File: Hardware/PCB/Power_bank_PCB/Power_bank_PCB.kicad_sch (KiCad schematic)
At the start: 86 parts, among them IC1 TPS63070RNMR, IC2 TPS63070RNMR, J1 Fotopanel_connector, J2 Vout, J3 Alterative_charging, Q1 8205A, Q2 2N7002, Q3 DMP3099L, U1 TP4056-42-ESOP8, U2 MCP4018-xxxxLT, U3 DW01A, U4 STM32U031F8Px, U5 INA219AxD, U6 TPS61022

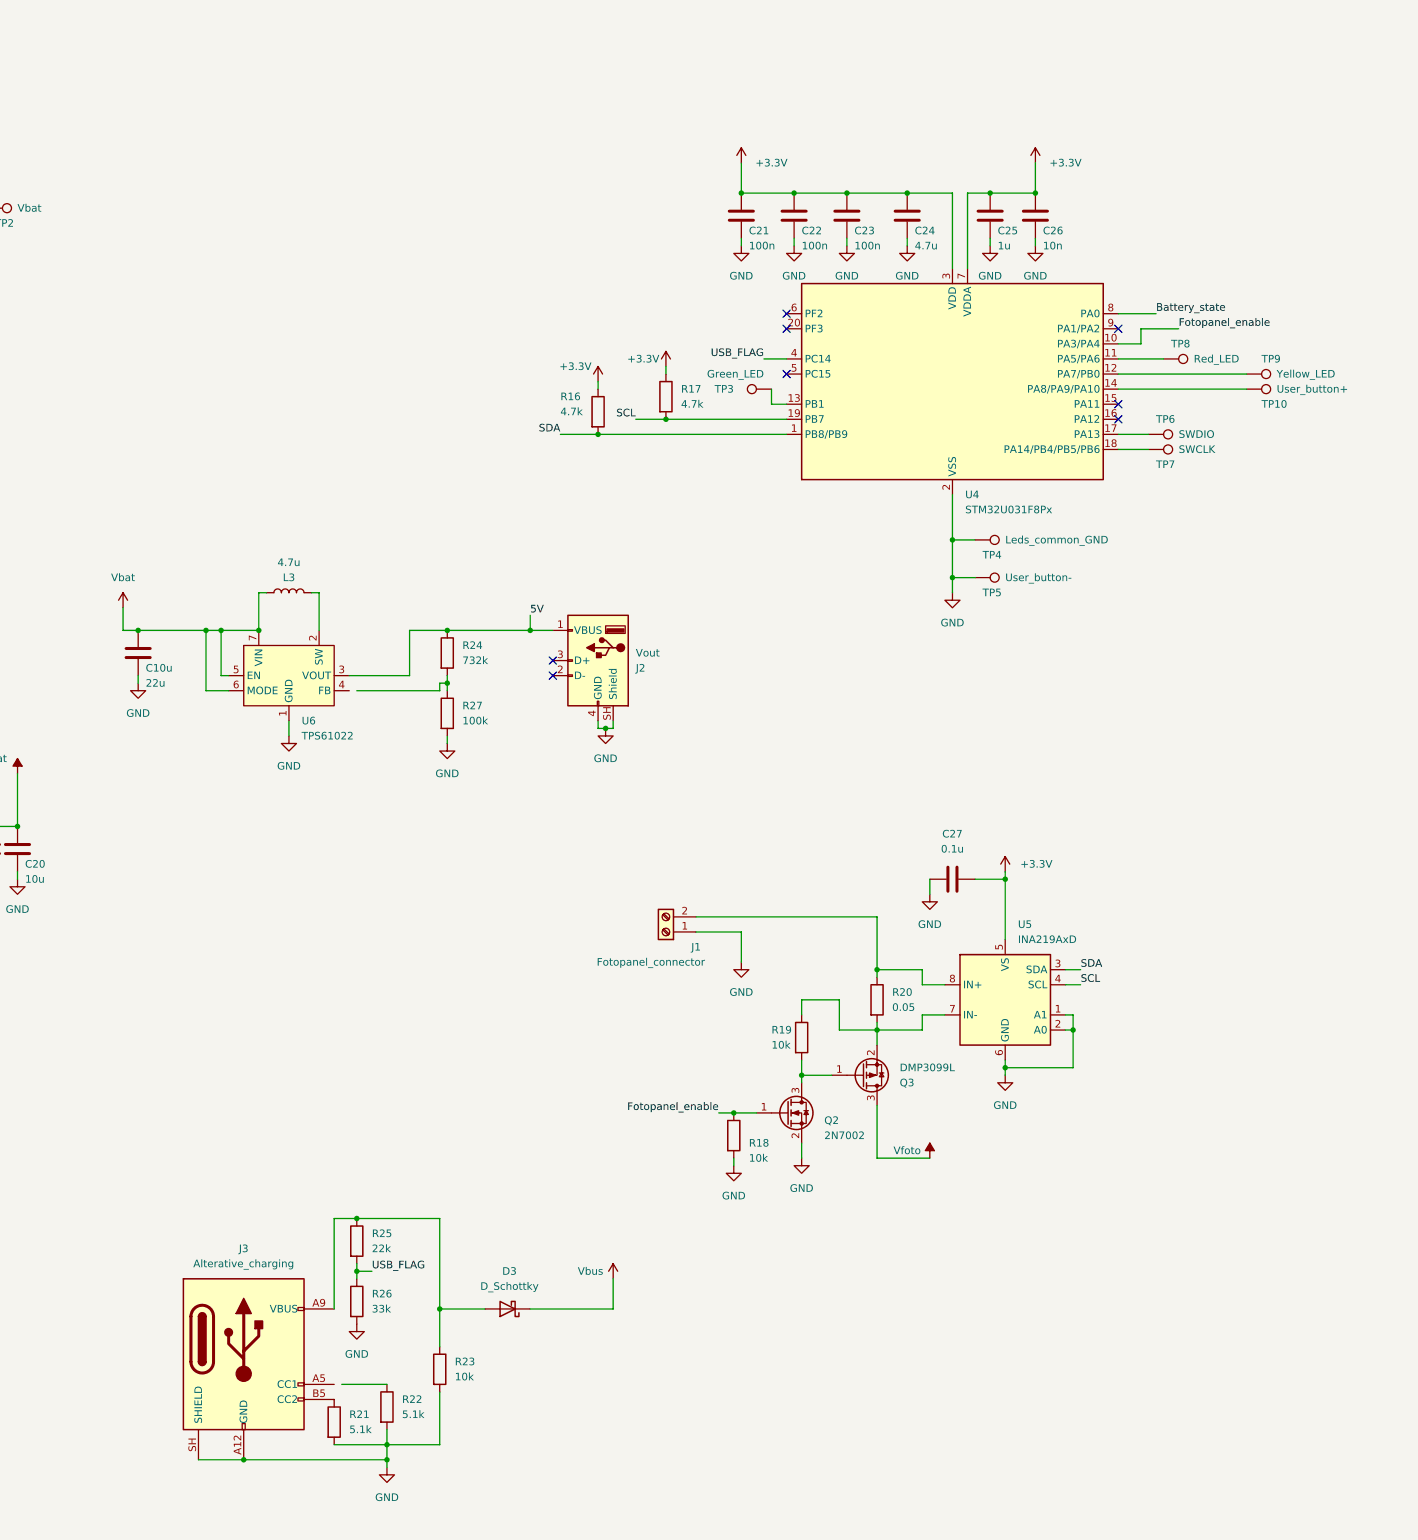
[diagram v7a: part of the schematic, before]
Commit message: Adjust schematic positions
Mass-update schematic component and net coordinates to match revised layout (many junctions, wires, labels and symbol positions changed). Add a +3.3V power symbol instance (#PWR064) and update used_designators (R21-29, D3-5, #PWR54-64, etc.). These changes align the schematic with the updated PCB placement and nets.
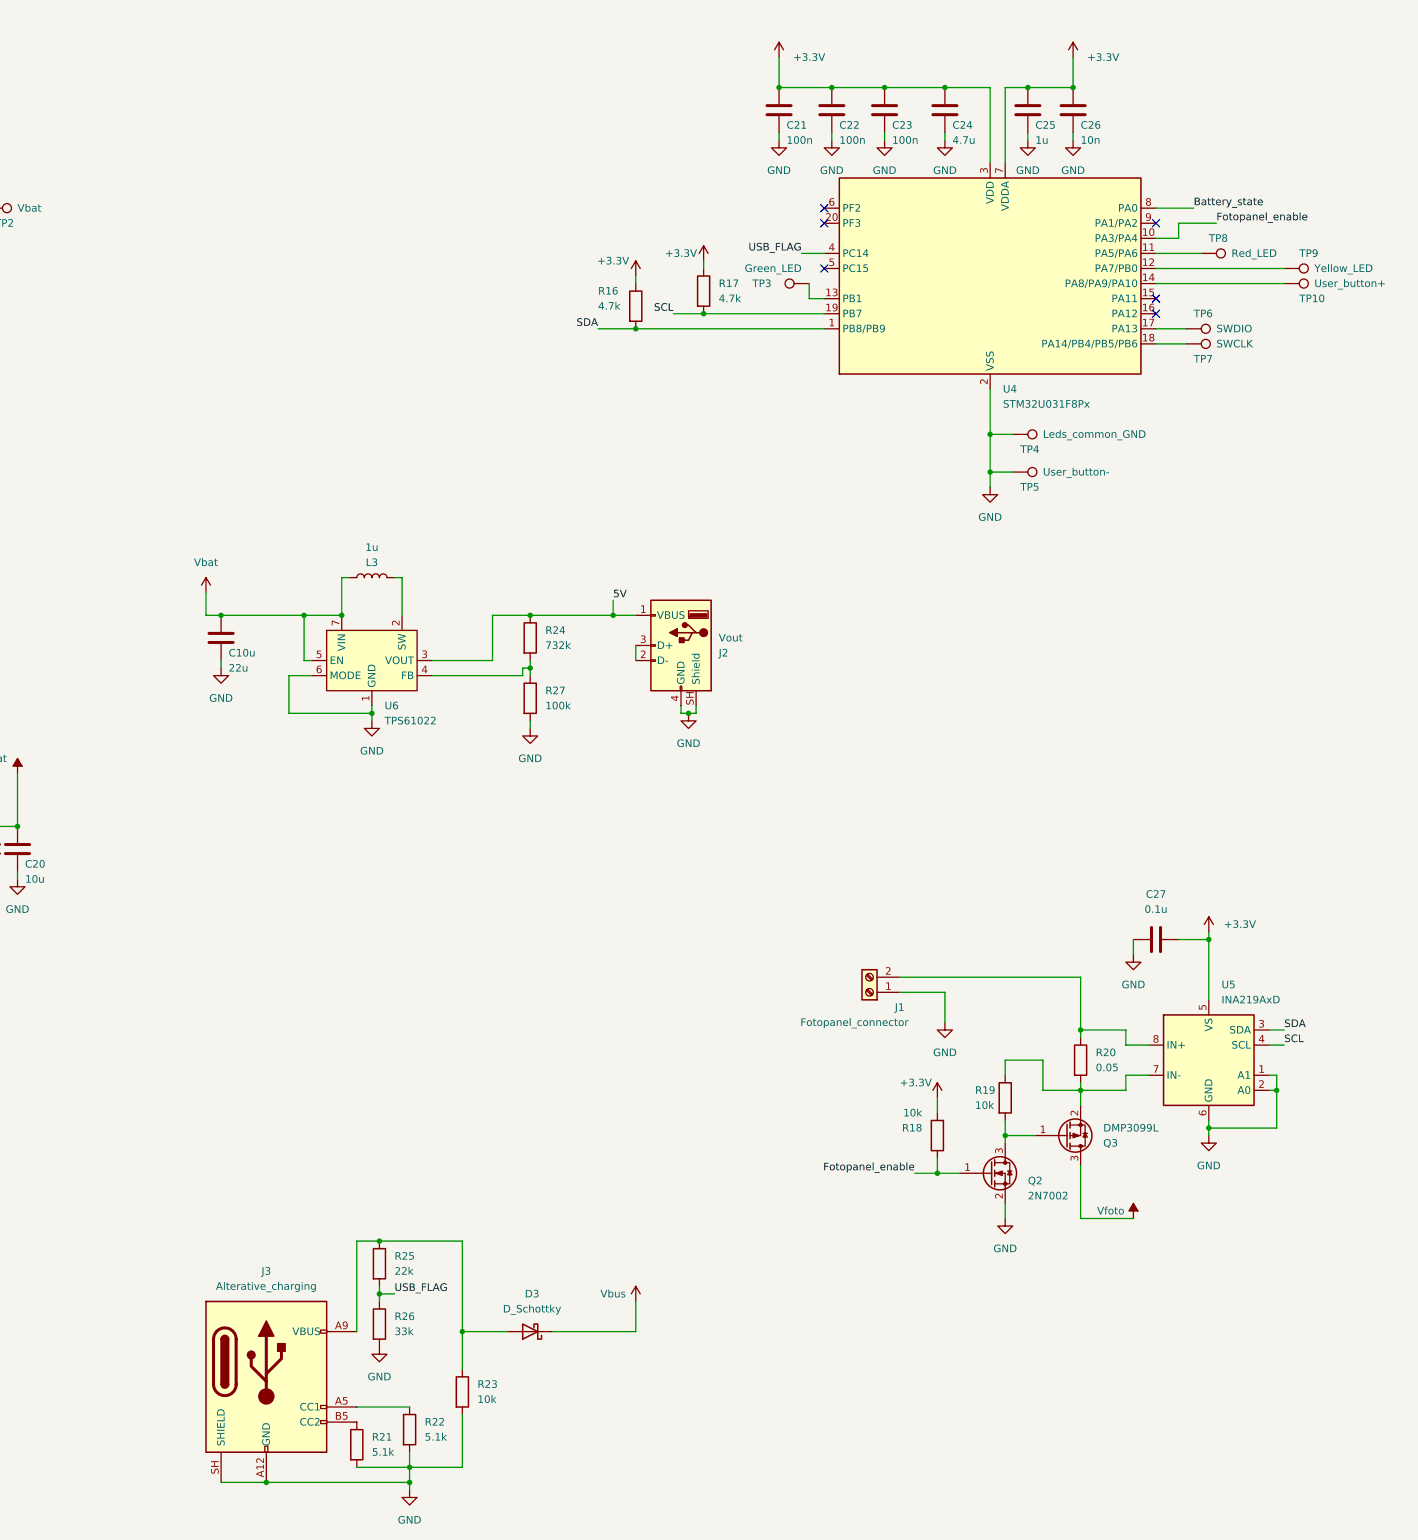
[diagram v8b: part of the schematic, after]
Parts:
- L3: value 4.7u -> 1u
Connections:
- net +3.3V: now also R18.2
- net GND: now also U6.6 (MODE); no longer R18.2
- net Vbat: no longer U6.6 (MODE)
- net at R24.2, R27.1: now also U6.4 (FB)
- net at R22.1: now also J3.A5 (CC1)
- net at J2.2 (D-): now also J2.3 (D+)
- no-connect marks 8 -> 6
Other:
- moved on the sheet: C10u, C21, C22, C23, C24, C25, C26, C27, D3, J1, J2, J3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
